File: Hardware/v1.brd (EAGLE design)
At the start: 35.6 x 35.6 mm, 33 parts, among them IC1 IC_FT2232H-56Q, IC3 IC_MAX3313, X1 6MHz

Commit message: a
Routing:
- net +1V8: track 25.4 -> 55.2 mm, vias 0 -> 3
- net GND: vias 0 -> 15
- added copper zone on layer 16, net GND
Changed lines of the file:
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@@
 <wire x1="43.18" y1="43.18" x2="7.62" y2="43.18" width="0" layer="20"/>
 <wire x1="7.62" y1="43.18" x2="7.62" y2="7.62" width="0" layer="20"/>
+<rectangle x1="18.288" y1="26.924" x2="21.844" y2="27.94" layer="42"/>
+<rectangle x1="13.208" y1="31.242" x2="17.526" y2="33.274" layer="42"/>
+<rectangle x1="17.526" y1="26.924" x2="19.05" y2="33.274" layer="42"/>
+<rectangle x1="22" y1="22" x2="30" y2="28" layer="41"/>
 </plain>
 <attributes>
@@
 </element>
 <element name="C11" library="rcl" package="C0603" value="100nF" x="15.24" y="29.972" smashed="yes" rot="R180">
-<attribute name="NAME" x="11.176" y="29.972" size="1.27" layer="25" font="vector" rot="R180" align="center"/>
+<attribute name="NAME" x="11.43" y="29.972" size="1.27" layer="25" font="vector" rot="R180" align="center"/>
 <attribute name="VALUE" x="15.24" y="31.877" size="1.27" layer="27" font="vector" rot="R180" align="center"/>
 </element>
@@
 <wire x1="24.13" y1="24.13" x2="25.4" y2="25.4" width="0.254" layer="1"/>
 <wire x1="27.65" y1="29.4" x2="27.65" y2="27.65" width="0.254" layer="1"/>
-<wire x1="27.65" y1="27.65" x2="27.432" y2="27.432" width="0.254" layer="1"/>
-<wire x1="27.432" y1="27.432" x2="25.4" y2="25.4" width="0.254" layer="1"/>
+<wire x1="27.65" y1="27.65" x2="25.4" y2="25.4" width="0.254" layer="1"/>
 <wire x1="29.4" y1="28.15" x2="28.15" y2="28.15" width="0.254" layer="1"/>
 <wire x1="28.15" y1="28.15" x2="27.65" y2="27.65" width="0.254" layer="1"/>
+<polygon width="0.254" layer="16">
+<vertex x="0.508" y="-0.254"/>
+<vertex x="247.65" y="-0.254"/>
+<vertex x="247.65" y="117.856"/>
+<vertex x="0.254" y="117.856"/>
+<vertex x="0.254" y="2.54"/>
+</polygon>
+<via x="27.178" y="30.734" extent="1-16" drill="0.4"/>
+<via x="30.48" y="28.194" extent="1-16" drill="0.4"/>
+<via x="25.146" y="20.32" extent="1-16" drill="0.4"/>
+<via x="25.4" y="25.4" extent="1-16" drill="0.4"/>
+<via x="23.4" y="25.4" extent="1-16" drill="0.4"/>
+<via x="23.4" y="27.4" extent="1-16" drill="0.4"/>
+<via x="25.4" y="27.4" extent="1-16" drill="0.4"/>
+<via x="27.4" y="27.4" extent="1-16" drill="0.4"/>
+<via x="27.4" y="25.4" extent="1-16" drill="0.4"/>
+<via x="27.4" y="23.4" extent="1-16" drill="0.4"/>
+<via x="25.4" y="23.4" extent="1-16" drill="0.4"/>
+<via x="23.4" y="23.4" extent="1-16" drill="0.4"/>
+<via x="15.24" y="34.036" extent="1-16" drill="0.4"/>
+<via x="14.224" y="34.036" extent="1-16" drill="0.4"/>
+<via x="16.256" y="34.036" extent="1-16" drill="0.4"/>
 <wire x1="-23.942" y1="19.304" x2="-29.022" y2="19.304" width="0" layer="19" extent="1-1"/>
 <wire x1="-23.26" y1="13.7" x2="-23.942" y2="19.304" width="0" layer="19" extent="1-1"/>
 <wire x1="14.39" y1="25.4" x2="-23.942" y2="19.304" width="0" layer="19" extent="1-1"/>
-<wire x1="29.4" y1="28.15" x2="36.41" y2="27.686" width="0" layer="19" extent="1-1"/>
 </signal>
 <signal name="+5V">
@@
 <contactref element="C10" pad="1"/>
 <contactref element="C9" pad="1"/>
-<wire x1="21.4" y1="28.15" x2="19.348" y2="28.15" width="0.254" layer="1"/>
-<wire x1="19.348" y1="28.15" x2="18.796" y2="28.702" width="0.254" layer="1"/>
-<wire x1="18.796" y1="28.702" x2="18.796" y2="33.528" width="0.254" layer="1"/>
 <wire x1="18.796" y1="33.528" x2="18.542" y2="33.782" width="0.254" layer="1"/>
 <wire x1="18.542" y1="33.782" x2="18.542" y2="34.71" width="0.254" layer="1"/>
@@
 <wire x1="28.65" y1="29.4" x2="28.65" y2="29.92" width="0.254" layer="1"/>
 <wire x1="29.4" y1="23.15" x2="30.19" y2="23.15" width="0.254" layer="1"/>
-<wire x1="30.19" y1="23.15" x2="32.766" y2="20.574" width="0.254" layer="1"/>
+<wire x1="30.988" y1="22.352" x2="32.766" y2="20.574" width="0.254" layer="1"/>
 <wire x1="32.766" y1="20.574" x2="32.766" y2="19.304" width="0.254" layer="1"/>
 <wire x1="32.766" y1="19.304" x2="33.528" y2="18.542" width="0.254" layer="1"/>
 <wire x1="33.528" y1="18.542" x2="34.71" y2="18.542" width="0.254" layer="1"/>
-<wire x1="30.19" y1="23.15" x2="33.782" y2="27.686" width="0" layer="19" extent="1-1"/>
-<wire x1="21.4" y1="28.15" x2="28.65" y2="29.4" width="0" layer="19" extent="1-1"/>
+<wire x1="21.4" y1="28.15" x2="19.348" y2="28.15" width="0.254" layer="1"/>
+<wire x1="19.348" y1="28.15" x2="18.796" y2="28.702" width="0.254" layer="1"/>
+<wire x1="18.796" y1="28.702" x2="18.796" y2="33.528" width="0.254" layer="1"/>
+<wire x1="18.796" y1="33.528" x2="19.05" y2="33.782" width="0.254" layer="1"/>
+<wire x1="19.05" y1="33.782" x2="19.304" y2="33.782" width="0.254" layer="1"/>
+<wire x1="19.304" y1="33.782" x2="19.558" y2="33.528" width="0.254" layer="1"/>
+<via x="19.558" y="33.528" extent="1-16" drill="0.4"/>
+<wire x1="19.558" y1="33.528" x2="32.766" y2="33.528" width="0.254" layer="16"/>
+<wire x1="32.766" y1="33.528" x2="33.274" y2="33.02" width="0.254" layer="16"/>
+<wire x1="33.274" y1="33.02" x2="33.274" y2="28.194" width="0.254" layer="16"/>
+<wire x1="33.274" y1="28.194" x2="32.766" y2="27.686" width="0.254" layer="16"/>
+<via x="32.766" y="27.686" extent="1-16" drill="0.4"/>
+<wire x1="32.766" y1="27.686" x2="33.274" y2="28.194" width="0.254" layer="1"/>
+<wire x1="30.19" y1="23.15" x2="30.988" y2="22.352" width="0.254" layer="1"/>
+<wire x1="30.988" y1="22.352" x2="30.988" y2="21.082" width="0.254" layer="1"/>
+<via x="30.988" y="21.082" extent="1-16" drill="0.4"/>
+<wire x1="30.988" y1="21.082" x2="30.988" y2="25.908" width="0.254" layer="16"/>
+<wire x1="30.988" y1="25.908" x2="32.766" y2="27.686" width="0.254" layer="16"/>
 </signal>
 <signal name="N$12">

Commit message: added eeprom and expanded sch
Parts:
- added C13: 100nF, rcl:C0603
- added C14: 10uF, rcl:C0603
- added CN1: (no value), m0wut:CONN_AMP_MUSB_K152
- added IC2: 93LC46AT-I/OT, Microchip_By_element14_Batch_1:SOT95P280X145-6N
- C3, C4, C5: device rcl:C0805 -> rcl:C0603
- LD1, LD2: device adafruit:CHIP-LED0603 -> adafruit:LED3MM
- moved LD1 6.24 mm to (38.5, 15.2), flipped to the bottom, turned to 270 degrees
- moved LD2 5.00 mm to (38.5, 36.3), flipped to the bottom, turned to 90 degrees
- moved C4 4.34 mm to (-23.4, 23.4)
- moved C10 3.05 mm to (15.5, 35.6)
- moved C12 3.05 mm to (15.5, 15.2)
- moved C2 3.05 mm to (32.5, 25.4)
- moved C6 3.05 mm to (32.5, 30.0)
- moved C7 3.05 mm to (32.5, 27.7)
- moved C8 3.05 mm to (26.9, 35.6)
- moved C9 3.05 mm to (32.5, 18.5)
- moved R10 3.05 mm to (20.1, 35.6)
- moved R13 3.05 mm to (26.9, 15.2)
- moved R14 3.05 mm to (29.2, 35.6)
- moved R5 3.05 mm to (20.1, 15.2)
- moved R7 3.05 mm to (32.5, 20.8)
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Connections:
- net CAT_RX renamed UART(K3_TO_PIC)
- net N$4 renamed RS232(PIC_TO_K3)
- net N$5 renamed RS232(K2_TO_PIC)
- removed net N$20: IC1.55, R12.2
- new net N$28: IC2.1, R12.1
- new net UART(CAT_TO_USB): R6.2
- new net UART(PIC_TO_K3): IC3.4
- new net UART(USB_TO_CAT): R5.2
- new net UART(USB_TO_WK): R7.2
- new net UART(WK_TO_USB): R8.2
- new net USB_N: CN1.2, R3.1
- new net USB_P: CN1.3, R4.1
- new net VCC: CN1.1
- net +3V3: now also C13.1, C14.1, IC2.6
- net GND: now also C13.2, C14.2, CN1.5, CN1.GND1, CN1.GND2, IC2.2
- net N$18: now also IC2.5
- net N$19: now also IC2.4
- net N$21: now also IC1.55, IC2.3, R12.2; no longer R12.1
- net N$24: now also LD1.K; no longer LD1.C
- net N$25: now also LD2.K; no longer LD2.C
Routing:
- net N$21: track 3.59 -> 27.9 mm, vias 0 -> 2
- net N$18: track 7.74 -> 26.1 mm, vias 0 -> 2
- net N$28: track 0.00 -> 18.1 mm
- net N$19: track 5.71 -> 23.3 mm, vias 0 -> 2
- net USB_N: track 0.00 -> 12.5 mm
- net USB_P: track 0.00 -> 12.0 mm
- net N$24: track 2.29 -> 13.0 mm
- net N$20: track 9.63 -> 0.00 mm
- net +3V3: track 127.0 -> 134.1 mm
- net N$25: track 7.65 -> 13.2 mm, vias 0 -> 1
- net +1V8: track 55.2 -> 53.6 mm
- net GND: vias 15 -> 20
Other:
- board size 35.6 x 35.6 mm -> 50 x 50 mm
- board text added: "CAT"
- board text added: "WK"

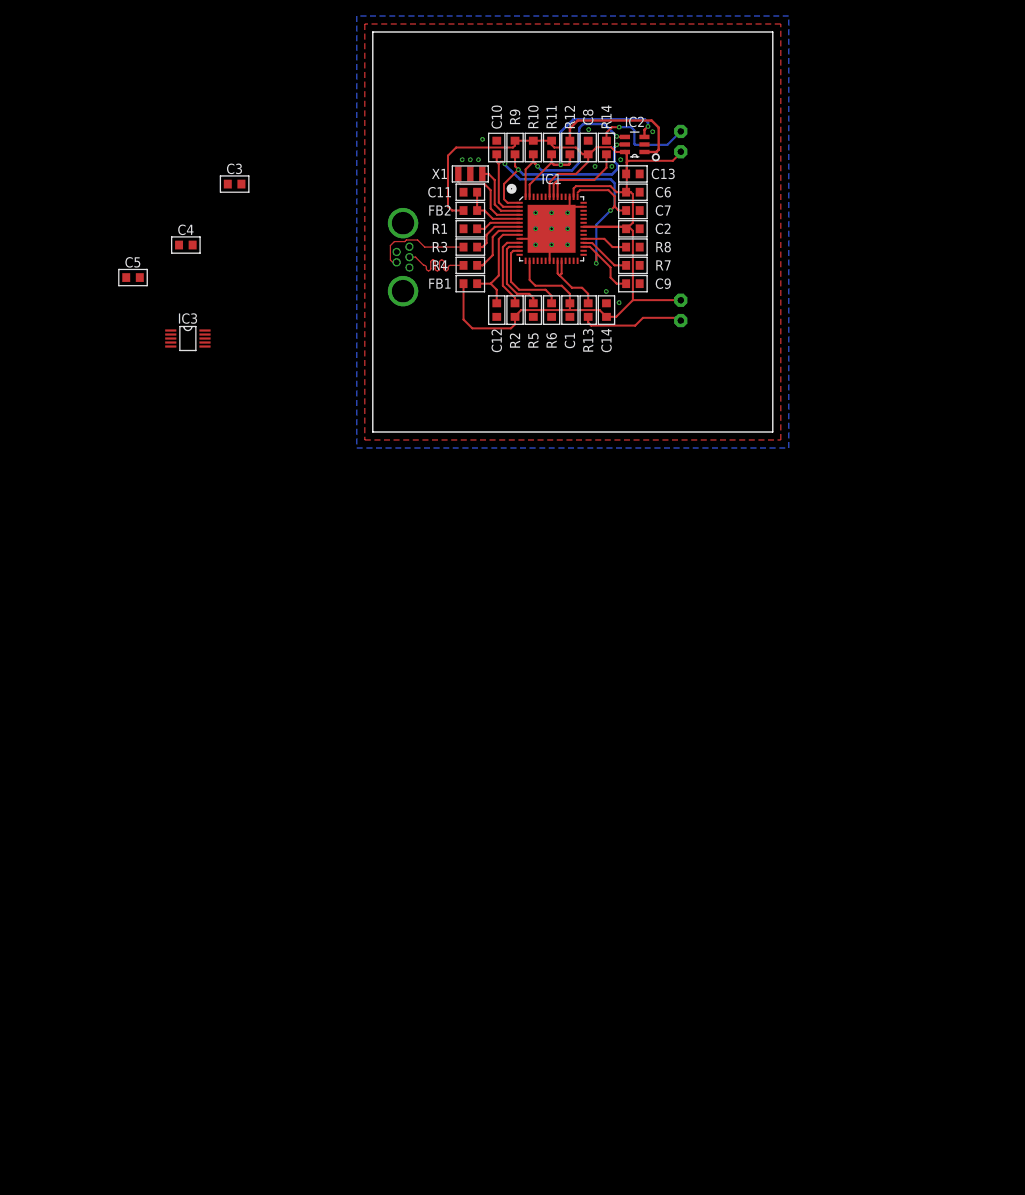
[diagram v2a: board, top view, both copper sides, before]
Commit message: Resized PCB now I have reference board
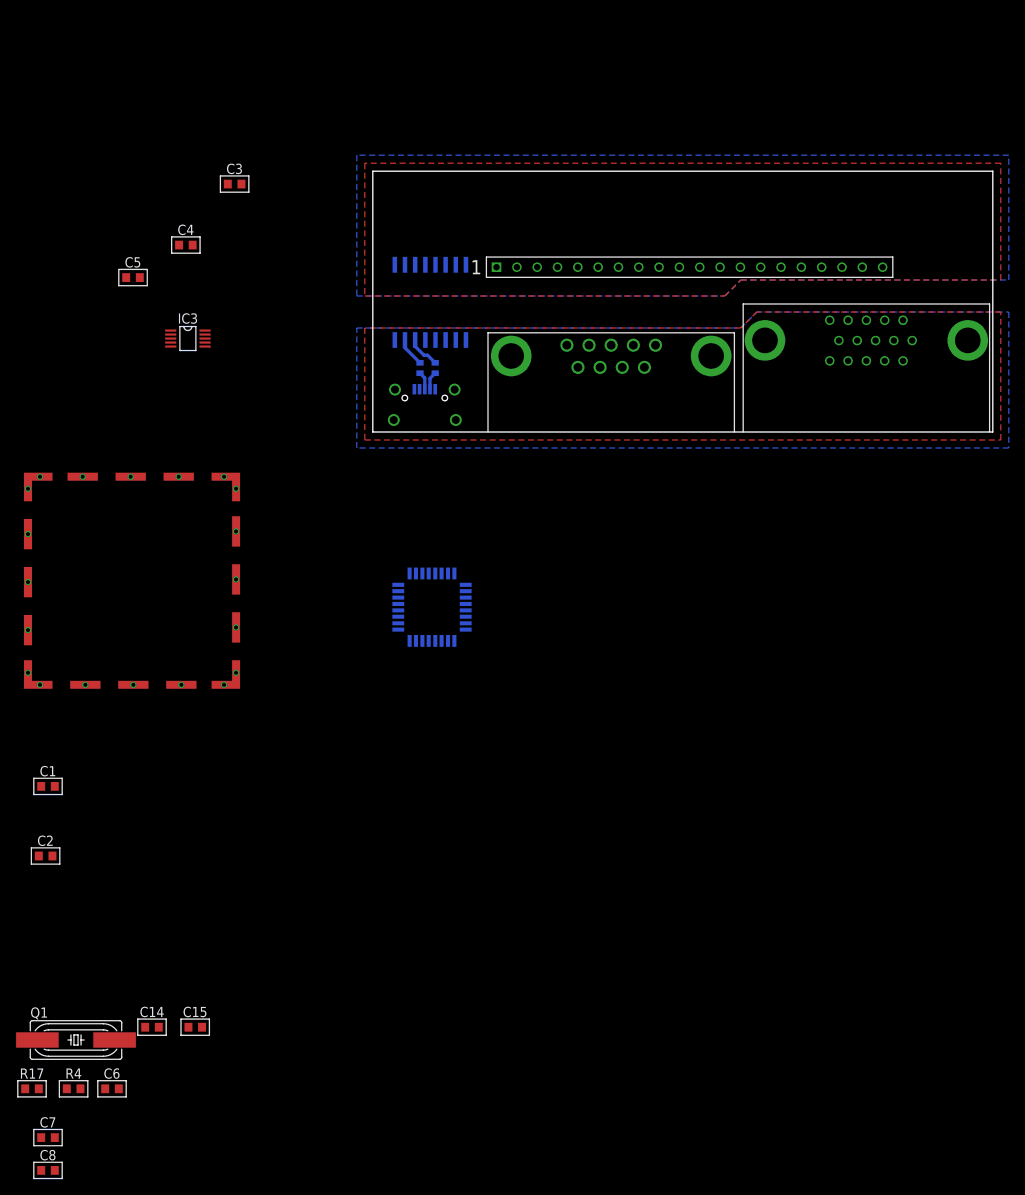
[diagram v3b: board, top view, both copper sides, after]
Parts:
- removed C10, C11, C12, C13, C9: 100nF, rcl:C0603
- removed FB1, FB2: FB0603, rcl:R0603
- removed IC2: 93LC46AT-I/OT, Microchip_By_element14_Batch_1:SOT95P280X145-6N
- removed LD1, LD2: (no value), adafruit:LED3MM
- removed R10, R11, R9: 10k, rcl:R0603
- removed R12: 2k2, rcl:R0603
- removed R13, R14, R5, R6, R7, R8: (no value), rcl:R0603
- removed R3: 27R, rcl:R0603
- removed X1: 6MHz, m0wut:XTAL_MURATA_3-PIN-RES
- added C15: 22pF, rcl:C0603
- added CAN1: CAN_LAIRD-BMI-S-203-F, m0wut:CAN_LAIRD_BMS-S-203-F
- added CN2: TSW-120-08-L-S-RA, m0wut:CONN_0.1_1X20
- added CN3: CONN_TE_DB9, m0wut:CONN_TE_DE9
- added CN4: CONN_TE_DB-HD15, m0wut:CONN_TE_DE-HD15
- added Q1: (no value), adafruit:HC49UP
- added R17: 1k5, rcl:R0603
- added U1: TUSB2036VF, Texas Instruments_By_element14_Batch_1:QFP80P900X900X145-32N
- C1, C2, C6, C8: value 100nF -> 1uF
- C14: value 10uF -> 22pF
- C7: value 3.3uF -> 1uF
- CN1: value (none) -> 629105150521; device m0wut:CONN_AMP_MUSB_K152 -> m0wut:USB_MICROB_WURTH
- IC1: value IC_FT2232H-56Q -> ADUM3160BRWZ; device m0wut:VQFN56 -> m0wut:SOIC127P1032X265-16N
- R1: value 12k -> 24; device rcl:R0603 -> rcl:R0402
- R2: value 1k -> 24; device rcl:R0603 -> rcl:R0402
- R4: value 27R -> 15k
- moved C8 144.6 mm to (-40.6, -92.3), turned to 0 degrees
- moved C7 137.0 mm to (-40.6, -88.2)
- moved C6 129.6 mm to (-32.6, -82.1)
- moved R4 114.3 mm to (-37.4, -82.1)
- moved C2 107.4 mm to (-40.9, -53.0)
- moved C14 106.1 mm to (-27.6, -74.4), turned to 0 degrees
- moved C1 88.3 mm to (-40.6, -44.3), turned to 0 degrees
- moved CN1 22.8 mm to (6.50, 0.00), turned to 0 degrees
- moved R1 18.5 mm to (5.90, 8.00), flipped to the bottom, turned to 90 degrees
- moved IC1 17.7 mm to (7.20, 16.2), flipped to the bottom, turned to 90 degrees
- moved R2 12.3 mm to (7.80, 8.00), flipped to the bottom
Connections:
- removed net +1V8: C10.1, C7.1, C9.1, IC1.2, IC1.31, IC1.43
- removed net N$12: C11.1, FB2.2, IC1.5
- removed net N$13: C12.1, FB1.2, IC1.9
- removed net N$14: IC1.12, R5.1
- removed net N$15: IC1.13, R6.1
- removed net N$16: IC1.32, R7.1
- removed net N$17: IC1.33, R8.1
- removed net N$18: IC1.1, IC2.5, R9.1
- removed net N$19: IC1.56, IC2.4, R10.1
- removed net N$21: IC1.55, IC2.3, R11.1, R12.2
- removed net N$22: IC1.23, IC1.24, R13.1
- removed net N$23: IC1.48, IC1.49, R14.1
- removed net N$24: LD1.K, R13.2
- removed net N$25: LD2.K, R14.2
- removed net N$28: IC2.1, R12.1
- removed net UART(CAT_TO_USB): R6.2
- removed net UART(USB_TO_CAT): R5.2
- removed net UART(USB_TO_WK): R7.2
- removed net UART(WK_TO_USB): R8.2
- removed net USB_N: CN1.2, R3.1
- removed net USB_P: CN1.3, R4.1
- removed net VCC: CN1.1
- new net AGND: C1.2, C2.2, CN1.5, CN1.GND1, CN1.GND2, CN1.GND3, CN1.GND4, IC1.2, IC1.8
- new net DM0: IC1.11, U1.2
- new net DM1: U1.11
- new net DM2: U1.15
- new net DM3: U1.19
- new net DP0: IC1.10, U1.1
- new net DP0PUR: U1.27
- new net DP1: U1.12
- new net DP2: U1.16
- new net DP3: U1.20
- new net N$4: IC1.7, R1.2
- new net N$5: C1.1, CN1.1, IC1.1
- new net XTAL1: C14.1, Q1.1, U1.30
- new net XTAL2: R17.2, U1.29
- net +3V3: now also C7.1, IC1.12, IC1.13, IC1.14, R4.1, U1.10, U1.14, U1.18, U1.24, U1.25, U1.26, U1.3, U1.8; no longer C1.1, C13.1, C14.1, C2.1, C6.1, FB1.1, FB2.1, IC1.36, IC1.44, IC1.50, IC2.6, LD1.A, LD2.A, R10.2, R11.2, R2.1, R9.2
- net GND: now also C15.2, C6.1, CAN1.P$1, CAN1.P$10, CAN1.P$11, CAN1.P$12, CAN1.P$13, CAN1.P$14, CAN1.P$15, CAN1.P$16, CAN1.P$17, CAN1.P$18, CAN1.P$19, CAN1.P$2, CAN1.P$20, CAN1.P$21, CAN1.P$22, CAN1.P$23, CAN1.P$24, CAN1.P$25, CAN1.P$26, CAN1.P$27, CAN1.P$28, CAN1.P$29, CAN1.P$3, CAN1.P$30, CAN1.P$31, CAN1.P$32, CAN1.P$33, CAN1.P$34, CAN1.P$35, CAN1.P$36, CAN1.P$37, CAN1.P$38, CAN1.P$39, CAN1.P$4, CAN1.P$40, CAN1.P$5, CAN1.P$6, CAN1.P$7, CAN1.P$8, CAN1.P$9, IC1.15, IC1.9, U1.21, U1.22, U1.23, U1.28, U1.31, U1.6, U1.7; no longer C1.2, C10.2, C11.2, C12.2, C13.2, C2.2, C6.2, C9.2, CN1.5, CN1.GND1, CN1.GND2, IC1.10, IC1.21, IC1.41, IC1.45, IC1.PAD, IC2.2, R1.1, X1.GND
- net N$1: now also CN1.3, R1.1; no longer IC1.3, X1.2
- net N$10: now also C6.2, R4.2, U1.4; no longer IC1.7, R3.2
- net N$11: now also C15.1, Q1.2, R17.1; no longer IC1.8, R4.2
- net N$2: now also CN1.2, R2.1; no longer IC1.4, X1.1
- net N$3: now also R2.2; no longer R1.2
- net N$9: now also C2.1, IC1.3, IC1.4, IC1.5; no longer IC1.11, R2.2
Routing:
- net +3V3: track 134.1 -> 0.00 mm
- net +1V8: track 53.6 -> 0.00 mm, vias 3 -> 0
- net N$21: track 27.9 -> 0.00 mm, vias 2 -> 0
- net N$18: track 26.1 -> 0.00 mm, vias 2 -> 0
- net N$19: track 23.3 -> 0.00 mm, vias 2 -> 0
- net N$28: track 18.1 -> 0.00 mm
- net GND: track 15.5 -> 0.00 mm, vias 20 -> 0
- net N$13: track 13.3 -> 0.00 mm
- net N$25: track 13.2 -> 0.00 mm, vias 1 -> 0
- net N$24: track 13.0 -> 0.00 mm
- net N$23: track 12.7 -> 0.00 mm
- net USB_N: track 12.5 -> 0.00 mm
- net USB_P: track 12.0 -> 0.00 mm
- net N$15: track 11.5 -> 0.00 mm
- net N$14: track 10.7 -> 0.00 mm
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- added copper zone on layer 1, net AGND
- added copper zone on layer 16, net AGND
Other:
- board size 50 x 50 mm -> 77.5 x 32.6 mm
- board text added: "Bottom clearance 9.5mm to top of audio board connector"
- board text removed: "CAT"
- board text removed: "WK"
